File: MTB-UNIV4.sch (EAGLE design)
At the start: 141 parts, among them IC1 MEGA128-A, IC2 SN75176BP, IC3 MC7805CDTG, IC4 ULN2803A, IC5 ULN2803A, X1A ARK500/2, X1B ARK500/2, X2A ARK500/2, X2B ARK500/2, X3 1751316, X4 1751316, X5 1751316, X6 1751316

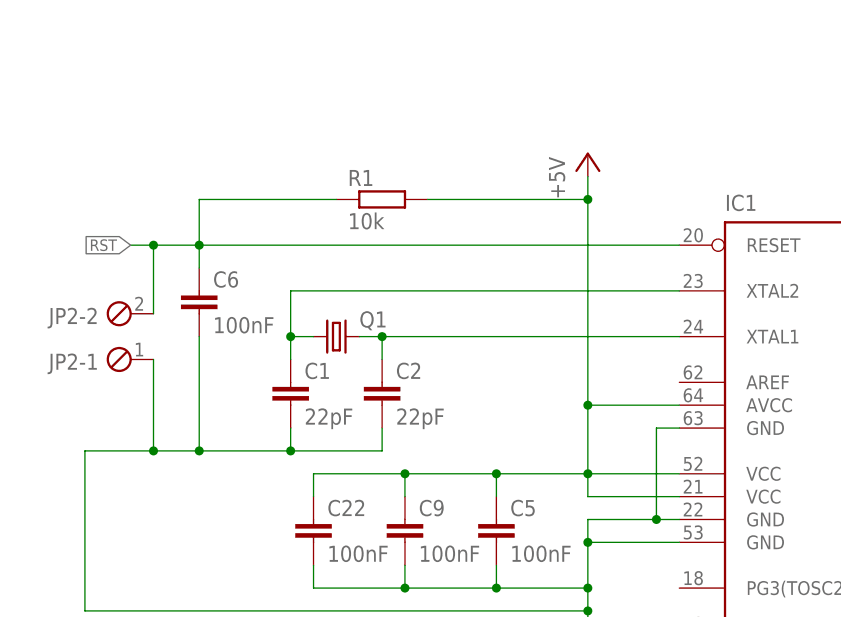
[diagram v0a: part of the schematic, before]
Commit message: Remove reset.
Reset could be done via programming connector.
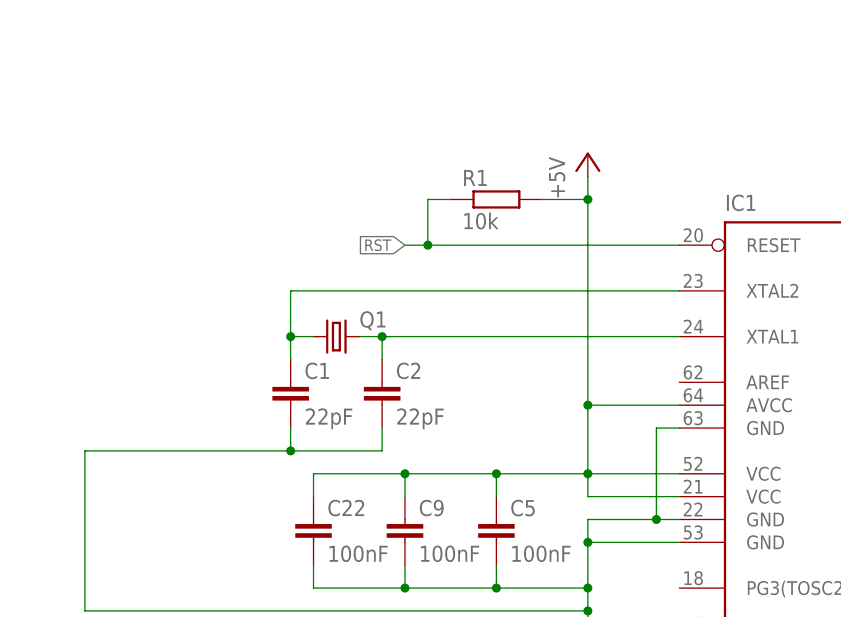
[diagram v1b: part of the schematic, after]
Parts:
- removed C6: 100nF, rcl:C-EUC1206
- removed JP2: (no value), con-phoenix-254:MPT2
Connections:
- net GND: no longer C6.2, JP2-1.1
- net RST: no longer C6.1, JP2-2.1
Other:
- moved on the sheet: R1
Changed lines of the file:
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@@
 <part name="C5" library="rcl" deviceset="C-EU" device="C1206" value="100nF"/>
 <part name="R1" library="rcl" deviceset="R-EU_" device="R1206" value="10k"/>
-<part name="C6" library="rcl" deviceset="C-EU" device="C1206" value="100nF"/>
 <part name="JPROG" library="adafruit" library_urn="urn:adsk.eagle:library:420" deviceset="AVRISP" device="-6" package3d_urn="urn:adsk.eagle:package:6240744/1"/>
 <part name="C7" library="rcl" deviceset="C-EU" device="C1206" value="100nF"/>
@@
 <part name="F1" library="adafruit_edited" deviceset="PTCFUSE" device="-1206" value="200mA"/>
 <part name="FRAME1" library="frames" library_urn="urn:adsk.eagle:library:229" deviceset="A3L-LOC" device=""/>
-<part name="JP2" library="con-phoenix-254" library_urn="urn:adsk.eagle:library:172" deviceset="MPT2" device="" package3d_urn="urn:adsk.eagle:package:9320/1"/>
 <part name="C11" library="rcl" library_urn="urn:adsk.eagle:library:334" deviceset="CPOL-EU" device="SMCB" package3d_urn="urn:adsk.eagle:package:25920/5" value="22uF"/>
 <part name="C10" library="rcl" library_urn="urn:adsk.eagle:library:334" deviceset="CPOL-EU" device="SMCD" package3d_urn="urn:adsk.eagle:package:25923/2" value="22uF"/>
@@
 <attribute name="VALUE" x="57.404" y="86.741" size="1.778" layer="96"/>
 </instance>
-<instance part="R1" gate="G$1" x="43.18" y="127" smashed="yes">
-<attribute name="NAME" x="39.37" y="128.4986" size="1.778" layer="95"/>
-<attribute name="VALUE" x="39.37" y="123.698" size="1.778" layer="96"/>
-</instance>
-<instance part="C6" gate="G$1" x="22.86" y="116.84" smashed="yes">
-<attribute name="NAME" x="24.384" y="117.221" size="1.778" layer="95"/>
-<attribute name="VALUE" x="24.384" y="112.141" size="1.778" layer="96"/>
+<instance part="R1" gate="G$1" x="55.88" y="127" smashed="yes">
+<attribute name="NAME" x="52.07" y="128.4986" size="1.778" layer="95"/>
+<attribute name="VALUE" x="52.07" y="123.698" size="1.778" layer="96"/>
 </instance>
 <instance part="JPROG" gate="G$1" x="304.8" y="106.68" smashed="yes">
@@
 <attribute name="LAST_DATE_TIME" x="344.17" y="10.16" size="2.286" layer="94"/>
 <attribute name="SHEET" x="357.505" y="5.08" size="2.54" layer="94"/>
-</instance>
-<instance part="JP2" gate="-1" x="15.24" y="109.22" smashed="yes" rot="R180">
-<attribute name="NAME" x="11.684" y="109.855" size="1.778" layer="95" rot="R180"/>
-</instance>
-<instance part="JP2" gate="-2" x="15.24" y="114.3" smashed="yes" rot="R180">
-<attribute name="NAME" x="11.684" y="114.935" size="1.778" layer="95" rot="R180"/>
-<attribute name="VALUE" x="16.256" y="117.602" size="1.778" layer="96" rot="R180"/>
 </instance>
 <instance part="C11" gate="G$1" x="358.14" y="55.88" smashed="yes">
@@
 <wire x1="43.18" y1="101.6" x2="43.18" y2="99.06" width="0.1524" layer="91"/>
 <wire x1="43.18" y1="99.06" x2="33.02" y2="99.06" width="0.1524" layer="91"/>
-<wire x1="33.02" y1="99.06" x2="22.86" y2="99.06" width="0.1524" layer="91"/>
-<wire x1="22.86" y1="99.06" x2="17.78" y2="99.06" width="0.1524" layer="91"/>
-<wire x1="17.78" y1="99.06" x2="10.16" y2="99.06" width="0.1524" layer="91"/>
+<wire x1="33.02" y1="99.06" x2="10.16" y2="99.06" width="0.1524" layer="91"/>
 <wire x1="10.16" y1="99.06" x2="10.16" y2="81.28" width="0.1524" layer="91"/>
 <pinref part="C1" gate="G$1" pin="2"/>
 <wire x1="33.02" y1="101.6" x2="33.02" y2="99.06" width="0.1524" layer="91"/>
 <junction x="33.02" y="99.06"/>
-<pinref part="C6" gate="G$1" pin="2"/>
-<wire x1="22.86" y1="111.76" x2="22.86" y2="99.06" width="0.1524" layer="91"/>
-<junction x="22.86" y="99.06"/>
-<pinref part="JP2" gate="-1" pin="1"/>
-<wire x1="17.78" y1="109.22" x2="17.78" y2="99.06" width="0.1524" layer="91"/>
-<junction x="17.78" y="99.06"/>
 <pinref part="C5" gate="G$1" pin="2"/>
 <wire x1="55.88" y1="86.36" x2="55.88" y2="83.82" width="0.1524" layer="91"/>
@@
 <junction x="66.04" y="104.14"/>
 <pinref part="R1" gate="G$1" pin="2"/>
-<wire x1="48.26" y1="127" x2="66.04" y2="127" width="0.1524" layer="91"/>
+<wire x1="60.96" y1="127" x2="66.04" y2="127" width="0.1524" layer="91"/>
 <junction x="66.04" y="127"/>
 <pinref part="C5" gate="G$1" pin="1"/>
@@
 <segment>
 <pinref part="R1" gate="G$1" pin="1"/>
-<pinref part="C6" gate="G$1" pin="1"/>
-<wire x1="38.1" y1="127" x2="22.86" y2="127" width="0.1524" layer="91"/>
-<wire x1="22.86" y1="127" x2="22.86" y2="121.92" width="0.1524" layer="91"/>
+<wire x1="50.8" y1="127" x2="48.26" y2="127" width="0.1524" layer="91"/>
+<wire x1="48.26" y1="127" x2="48.26" y2="121.92" width="0.1524" layer="91"/>
 <pinref part="IC1" gate="G$1" pin="RESET"/>
-<wire x1="22.86" y1="121.92" x2="22.86" y2="119.38" width="0.1524" layer="91"/>
-<wire x1="76.2" y1="121.92" x2="22.86" y2="121.92" width="0.1524" layer="91"/>
-<junction x="22.86" y="121.92"/>
-<wire x1="17.78" y1="121.92" x2="22.86" y2="121.92" width="0.1524" layer="91"/>
-<wire x1="15.24" y1="121.92" x2="17.78" y2="121.92" width="0.1524" layer="91"/>
-<junction x="17.78" y="121.92"/>
-<label x="15.24" y="121.92" size="1.27" layer="95" rot="R180" xref="yes"/>
-<pinref part="JP2" gate="-2" pin="1"/>
-<wire x1="17.78" y1="114.3" x2="17.78" y2="121.92" width="0.1524" layer="91"/>
+<wire x1="76.2" y1="121.92" x2="48.26" y2="121.92" width="0.1524" layer="91"/>
+<junction x="48.26" y="121.92"/>
+<wire x1="45.72" y1="121.92" x2="48.26" y2="121.92" width="0.1524" layer="91"/>
+<label x="45.72" y="121.92" size="1.27" layer="95" rot="R180" xref="yes"/>
 </segment>
 </net>

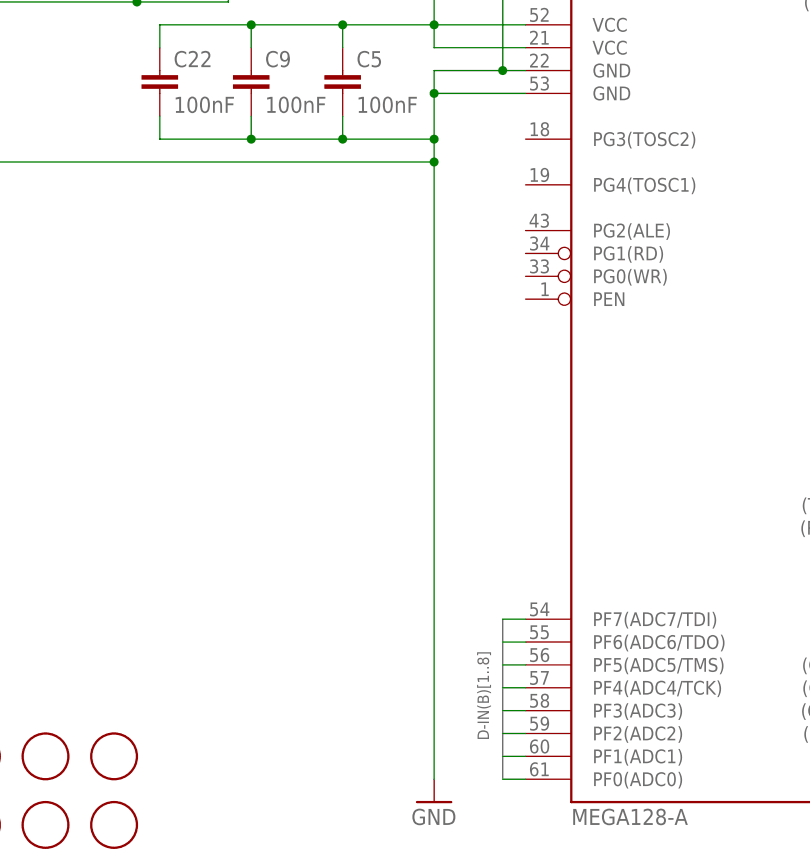
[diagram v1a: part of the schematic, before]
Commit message: Add a button.
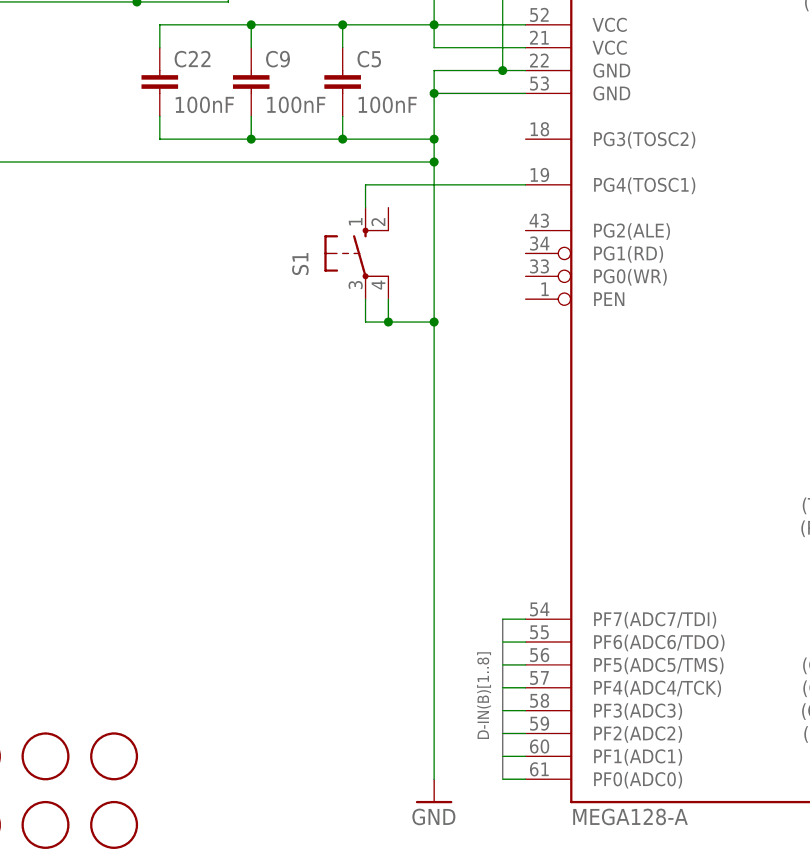
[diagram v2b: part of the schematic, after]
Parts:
- added S1: (no value), switch-omron:10-XX
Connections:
- new net N$86: IC1.PG4(TOSC1), S1.S
- net GND: now also S1.P, S1.P1
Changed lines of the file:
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@@
 <part name="U$7" library="adafruit" library_urn="urn:adsk.eagle:library:420" deviceset="FIDUCIAL" device="" package3d_urn="urn:adsk.eagle:package:6240632/1"/>
 <part name="U$8" library="adafruit" library_urn="urn:adsk.eagle:library:420" deviceset="FIDUCIAL" device="" package3d_urn="urn:adsk.eagle:package:6240632/1"/>
+<part name="S1" library="switch-omron" library_urn="urn:adsk.eagle:library:377" deviceset="10-XX" device="" package3d_urn="urn:adsk.eagle:package:27496/1"/>
 </parts>
 <sheets>
@@
 <instance part="U$7" gate="G$1" x="22.86" y="15.24" smashed="yes"/>
 <instance part="U$8" gate="G$1" x="30.48" y="15.24" smashed="yes"/>
+<instance part="S1" gate="1" x="58.42" y="71.12" smashed="yes">
+<attribute name="NAME" x="52.07" y="68.58" size="1.778" layer="95" rot="R90"/>
+<attribute name="VALUE" x="54.61" y="74.295" size="1.778" layer="96" rot="R90"/>
+</instance>
 </instances>
 <busses>
@@
 <pinref part="GND6" gate="1" pin="GND"/>
 <pinref part="IC1" gate="G$1" pin="GND"/>
-<wire x1="66.04" y1="12.7" x2="66.04" y2="81.28" width="0.1524" layer="91"/>
+<wire x1="66.04" y1="12.7" x2="66.04" y2="63.5" width="0.1524" layer="91"/>
+<wire x1="66.04" y1="63.5" x2="66.04" y2="81.28" width="0.1524" layer="91"/>
 <wire x1="66.04" y1="81.28" x2="66.04" y2="83.82" width="0.1524" layer="91"/>
 <wire x1="66.04" y1="83.82" x2="66.04" y2="88.9" width="0.1524" layer="91"/>
@@
 <wire x1="35.56" y1="83.82" x2="45.72" y2="83.82" width="0.1524" layer="91"/>
 <junction x="45.72" y="83.82"/>
+<wire x1="60.96" y1="63.5" x2="66.04" y2="63.5" width="0.1524" layer="91"/>
+<junction x="66.04" y="63.5"/>
+<pinref part="S1" gate="1" pin="P1"/>
+<wire x1="60.96" y1="63.5" x2="60.96" y2="66.04" width="0.1524" layer="91"/>
+<wire x1="60.96" y1="63.5" x2="58.42" y2="63.5" width="0.1524" layer="91"/>
+<junction x="60.96" y="63.5"/>
+<pinref part="S1" gate="1" pin="P"/>
+<wire x1="58.42" y1="63.5" x2="58.42" y2="66.04" width="0.1524" layer="91"/>
 </segment>
 <segment>
@@
 </segment>
 </net>
+<net name="N$86" class="0">
+<segment>
+<wire x1="58.42" y1="78.74" x2="76.2" y2="78.74" width="0.1524" layer="91"/>
+<pinref part="IC1" gate="G$1" pin="PG4(TOSC1)"/>
+<pinref part="S1" gate="1" pin="S"/>
+<wire x1="58.42" y1="78.74" x2="58.42" y2="76.2" width="0.1524" layer="91"/>
+</segment>
+</net>

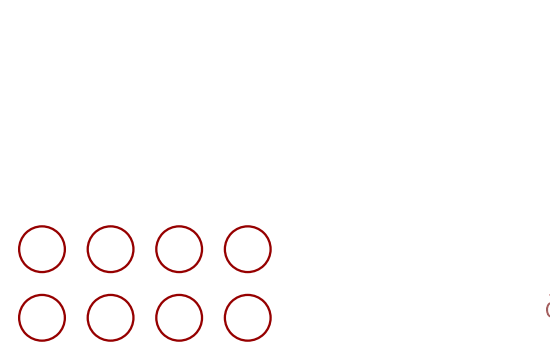
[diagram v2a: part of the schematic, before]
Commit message: Remove fiducials.
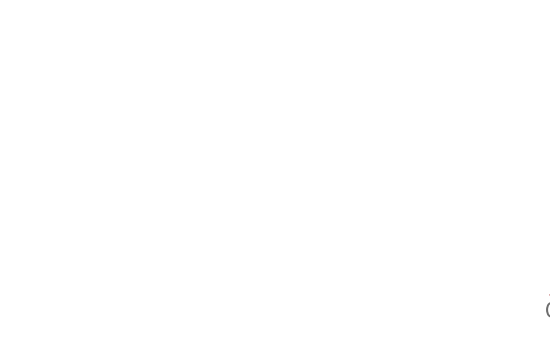
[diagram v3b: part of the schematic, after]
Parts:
- removed U$1, U$2, U$3, U$4, U$5, U$6, U$7, U$8: FIDUCIAL, adafruit:FIDUCIAL
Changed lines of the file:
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@@
 <part name="GND18" library="supply1" library_urn="urn:adsk.eagle:library:371" deviceset="GND" device=""/>
 <part name="GND19" library="supply1" library_urn="urn:adsk.eagle:library:371" deviceset="GND" device=""/>
-<part name="U$1" library="adafruit" library_urn="urn:adsk.eagle:library:420" deviceset="FIDUCIAL" device="" package3d_urn="urn:adsk.eagle:package:6240632/1"/>
-<part name="U$2" library="adafruit" library_urn="urn:adsk.eagle:library:420" deviceset="FIDUCIAL" device="" package3d_urn="urn:adsk.eagle:package:6240632/1"/>
-<part name="U$3" library="adafruit" library_urn="urn:adsk.eagle:library:420" deviceset="FIDUCIAL" device="" package3d_urn="urn:adsk.eagle:package:6240632/1"/>
-<part name="U$4" library="adafruit" library_urn="urn:adsk.eagle:library:420" deviceset="FIDUCIAL" device="" package3d_urn="urn:adsk.eagle:package:6240632/1"/>
 <part name="JP3" library="con-molex" deviceset="22-?-09" device="OCTHOLE"/>
 <part name="JP4" library="con-molex" deviceset="22-?-09" device="OCTHOLE"/>
@@
 <part name="R25" library="rcl" deviceset="R-EU_" device="R1206" value="10k"/>
 <part name="GND7" library="supply1" library_urn="urn:adsk.eagle:library:371" deviceset="GND" device=""/>
-<part name="U$5" library="adafruit" library_urn="urn:adsk.eagle:library:420" deviceset="FIDUCIAL" device="" package3d_urn="urn:adsk.eagle:package:6240632/1"/>
-<part name="U$6" library="adafruit" library_urn="urn:adsk.eagle:library:420" deviceset="FIDUCIAL" device="" package3d_urn="urn:adsk.eagle:package:6240632/1"/>
-<part name="U$7" library="adafruit" library_urn="urn:adsk.eagle:library:420" deviceset="FIDUCIAL" device="" package3d_urn="urn:adsk.eagle:package:6240632/1"/>
-<part name="U$8" library="adafruit" library_urn="urn:adsk.eagle:library:420" deviceset="FIDUCIAL" device="" package3d_urn="urn:adsk.eagle:package:6240632/1"/>
 <part name="S1" library="switch-omron" library_urn="urn:adsk.eagle:library:377" deviceset="10-XX" device="" package3d_urn="urn:adsk.eagle:package:27496/1"/>
 </parts>
@@
 <attribute name="VALUE" x="193.04" y="127" size="1.778" layer="96"/>
 </instance>
-<instance part="U$1" gate="G$1" x="7.62" y="7.62" smashed="yes"/>
-<instance part="U$2" gate="G$1" x="15.24" y="7.62" smashed="yes"/>
-<instance part="U$3" gate="G$1" x="22.86" y="7.62" smashed="yes"/>
-<instance part="U$4" gate="G$1" x="30.48" y="7.62" smashed="yes"/>
 <instance part="JP3" gate="-1" x="358.14" y="248.92" smashed="yes">
 <attribute name="NAME" x="360.68" y="248.158" size="1.524" layer="95"/>
@@
 <attribute name="VALUE" x="180.34" y="71.12" size="1.778" layer="96"/>
 </instance>
-<instance part="U$5" gate="G$1" x="7.62" y="15.24" smashed="yes"/>
-<instance part="U$6" gate="G$1" x="15.24" y="15.24" smashed="yes"/>
-<instance part="U$7" gate="G$1" x="22.86" y="15.24" smashed="yes"/>
-<instance part="U$8" gate="G$1" x="30.48" y="15.24" smashed="yes"/>
 <instance part="S1" gate="1" x="58.42" y="71.12" smashed="yes">
 <attribute name="NAME" x="52.07" y="68.58" size="1.778" layer="95" rot="R90"/>

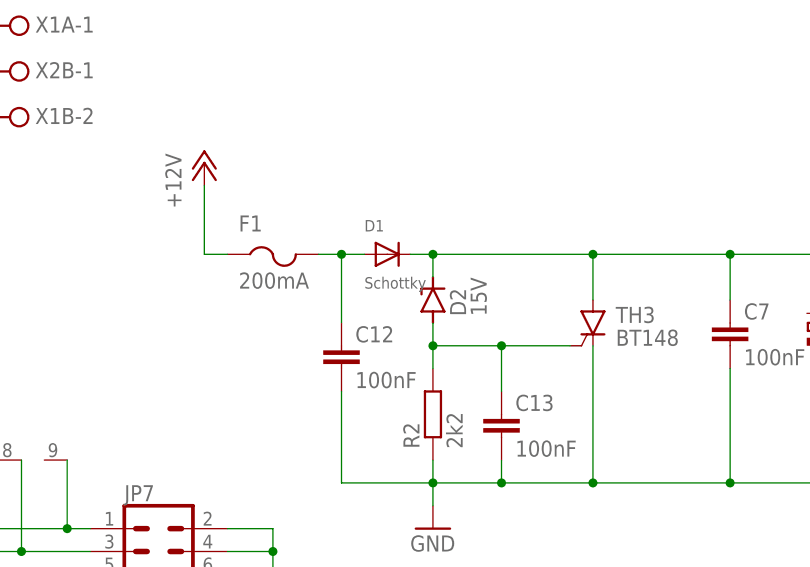
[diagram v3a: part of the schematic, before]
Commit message: Add Schottky diode value.
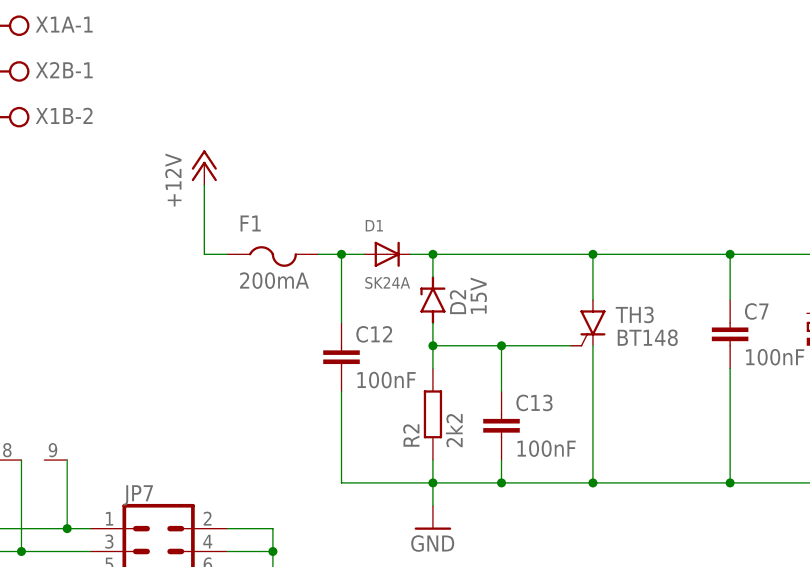
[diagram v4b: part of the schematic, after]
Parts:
- D1: value Schottky -> SK24A
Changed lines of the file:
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@@
 <part name="GND13" library="supply1" library_urn="urn:adsk.eagle:library:371" deviceset="GND" device=""/>
 <part name="GND14" library="supply1" library_urn="urn:adsk.eagle:library:371" deviceset="GND" device=""/>
-<part name="D1" library="adafruit" library_urn="urn:adsk.eagle:library:420" deviceset="DIODE" device="SMA" package3d_urn="urn:adsk.eagle:package:6240747/1" value="Schottky"/>
+<part name="D1" library="adafruit" library_urn="urn:adsk.eagle:library:420" deviceset="DIODE" device="SMA" package3d_urn="urn:adsk.eagle:package:6240747/1" value="SK24A"/>
 <part name="F1" library="adafruit_edited" deviceset="PTCFUSE" device="-1206" value="200mA"/>
 <part name="FRAME1" library="frames" library_urn="urn:adsk.eagle:library:229" deviceset="A3L-LOC" device=""/>

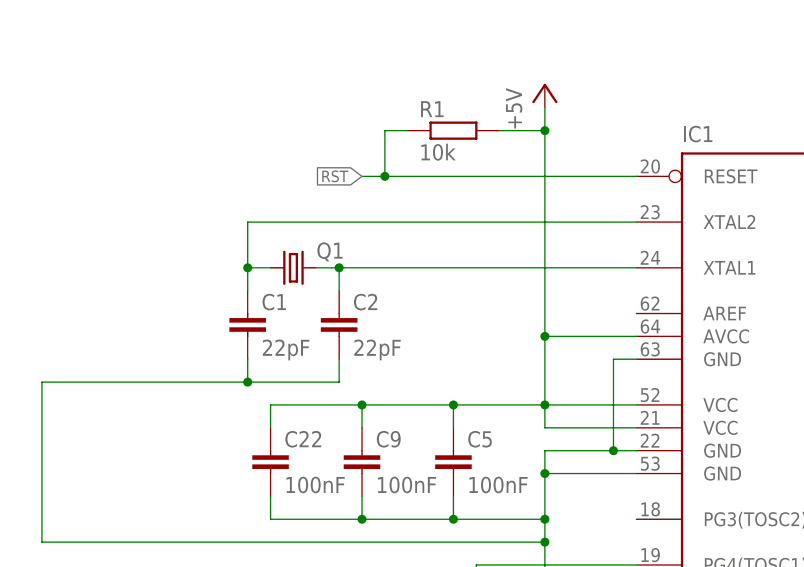
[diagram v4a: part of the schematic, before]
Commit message: Add crystal frequency.
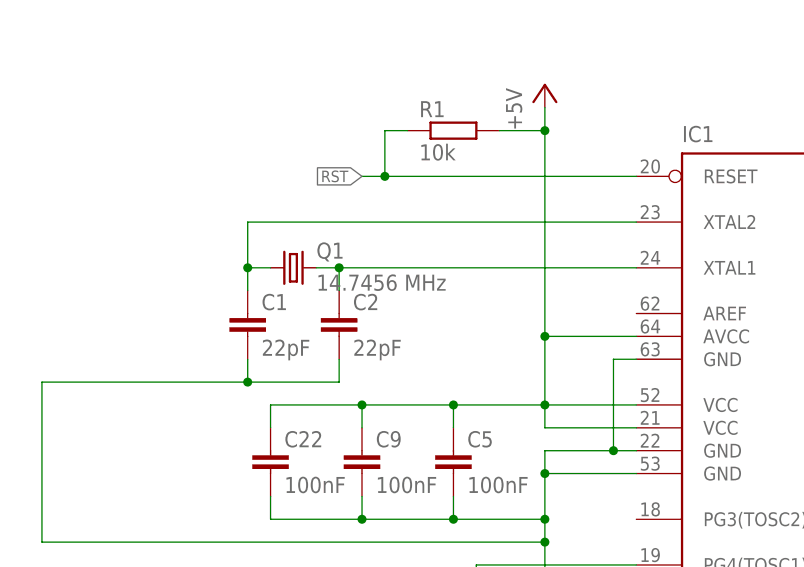
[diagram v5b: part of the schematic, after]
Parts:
- Q1: value (none) -> 14.7456 MHz
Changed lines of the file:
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@@
 </classes>
 <parts>
-<part name="Q1" library="crystal" library_urn="urn:adsk.eagle:library:204" deviceset="CRYSTAL" device="HC49S" package3d_urn="urn:adsk.eagle:package:12071/1"/>
+<part name="Q1" library="crystal" library_urn="urn:adsk.eagle:library:204" deviceset="CRYSTAL" device="HC49S" package3d_urn="urn:adsk.eagle:package:12071/1" value="14.7456 MHz"/>
 <part name="IC5" library="uln-udn" library_urn="urn:adsk.eagle:library:407" deviceset="ULN2803A" device="" package3d_urn="urn:adsk.eagle:package:16424/2" value="ULN2803A"/>
 <part name="IC4" library="uln-udn" library_urn="urn:adsk.eagle:library:407" deviceset="ULN2803A" device="" package3d_urn="urn:adsk.eagle:package:16424/2" value="ULN2803A"/>
